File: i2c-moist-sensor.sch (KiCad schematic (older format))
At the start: 21 parts, among them IC1 ATTINY441-SSU, P1 CONN_02X03, X1 16MHz

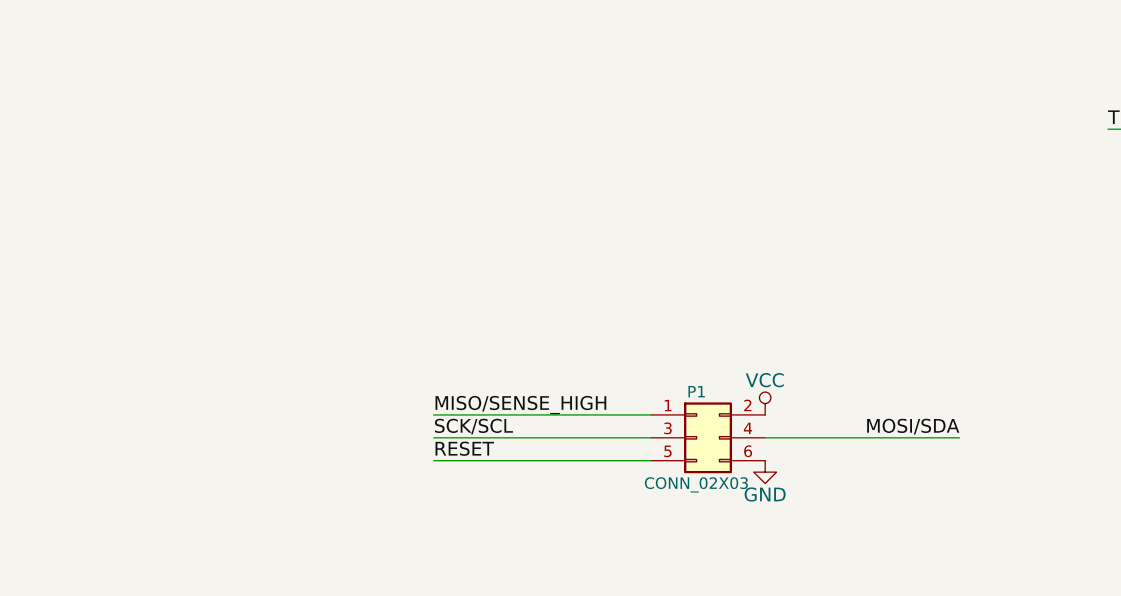
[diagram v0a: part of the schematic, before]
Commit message: Add Qwiic connectors
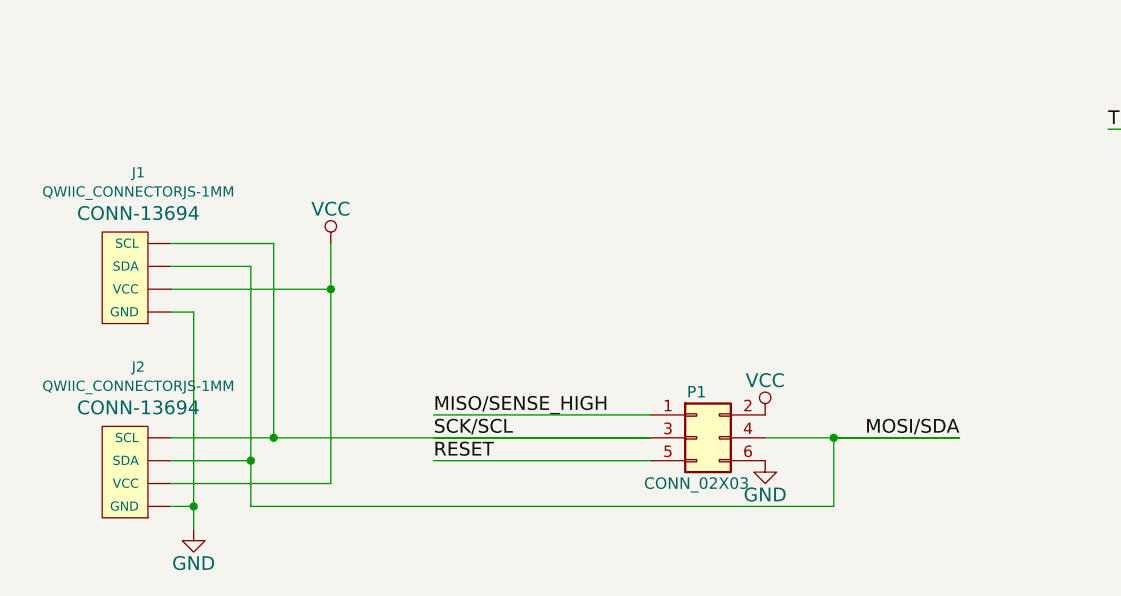
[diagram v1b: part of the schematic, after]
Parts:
- added J1, J2: QWIIC_CONNECTORJS-1MM, Connector_JST:JST_SH_SM04B-SRSS-TB_1x04-1MP_P1.00mm_Horizontal, symbol SparkFun-Connectors:QWIIC_CONNECTORJS-1MM
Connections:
- net GND: now also J1.1 (GND), J2.1 (GND)
- net MOSI/SDA: now also J1.3 (SDA), J2.3 (SDA)
- net SCK/SCL: now also J1.4 (SCL), J2.4 (SCL)
- net VCC: now also J1.2 (VCC), J2.2 (VCC)
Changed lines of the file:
@@
 	9600 3800 10500 3800
 Connection ~ 7250 4300
+$Comp
+L SparkFun-Connectors:QWIIC_CONNECTORJS-1MM J1
+U 1 1 5E00ADE6
+P 2050 5100
+F 0 "J1" H 2008 5710 45  0000 C CNN
+F 1 "QWIIC_CONNECTORJS-1MM" H 2008 5626 45  0000 C CNN
+F 2 "Connector_JST:JST_SH_SM04B-SRSS-TB_1x04-1MP_P1.00mm_Horizontal" H 2050 5600 20  0001 C CNN
+F 3 "" H 2050 5100 50  0001 C CNN
+F 4 "CONN-13694" H 2008 5531 60  0000 C CNN "Field4"
+	1    2050 5100
+	1    0    0    -1
+$EndComp
+$Comp
+L SparkFun-Connectors:QWIIC_CONNECTORJS-1MM J2
+U 1 1 5E00B3F3
+P 2050 5950
+F 0 "J2" H 2008 6560 45  0000 C CNN
+F 1 "QWIIC_CONNECTORJS-1MM" H 2008 6476 45  0000 C CNN
+F 2 "Connector_JST:JST_SH_SM04B-SRSS-TB_1x04-1MP_P1.00mm_Horizontal" H 2050 6450 20  0001 C CNN
+F 3 "" H 2050 5950 50  0001 C CNN
+F 4 "CONN-13694" H 2008 6381 60  0000 C CNN "Field4"
+	1    2050 5950
+	1    0    0    -1
+$EndComp
+$Comp
+L power:GND #PWR0101
+U 1 1 5E011E38
+P 2250 6050
+F 0 "#PWR0101" H 2250 5800 60  0001 C CNN
+F 1 "GND" H 2250 5900 60  0000 C CNN
+F 2 "" H 2250 6050 60  0000 C CNN
+F 3 "" H 2250 6050 60  0000 C CNN
+	1    2250 6050
+	1    0    0    -1
+$EndComp
+Wire Wire Line
+	2250 6050 2250 5950
+Wire Wire Line
+	2250 5950 2150 5950
+Wire Wire Line
+	2250 5950 2250 5100
+Wire Wire Line
+	2250 5100 2150 5100
+Connection ~ 2250 5950
+Wire Wire Line
+	2600 4800 2150 4800
+Wire Wire Line
+	2150 5650 2600 5650
+Wire Wire Line
+	5050 5650 5050 5950
+Wire Wire Line
+	5050 5950 2500 5950
+Wire Wire Line
+	2500 5950 2500 5750
+Wire Wire Line
+	2500 4900 2150 4900
+Connection ~ 5050 5650
+Wire Wire Line
+	5050 5650 5600 5650
+Wire Wire Line
+	2150 5750 2500 5750
+Connection ~ 2500 5750
+Wire Wire Line
+	2500 5750 2500 4900
+Wire Wire Line
+	2150 5850 2850 5850
+Wire Wire Line
+	2850 5850 2850 5000
+Wire Wire Line
+	2850 5000 2150 5000
+$Comp
+L power:VCC #PWR0102
+U 1 1 5E01C864
+P 2850 4800
+F 0 "#PWR0102" H 2850 4650 60  0001 C CNN
+F 1 "VCC" H 2850 4950 60  0000 C CNN
+F 2 "" H 2850 4800 60  0000 C CNN
+F 3 "" H 2850 4800 60  0000 C CNN
+	1    2850 4800
+	1    0    0    -1
+$EndComp
+Wire Wire Line
+	2850 4800 2850 5000
+Connection ~ 2850 5000
+Connection ~ 2600 5650
+Wire Wire Line
+	2600 4800 2600 5650
+Wire Wire Line
+	2600 5650 4250 5650
 Connection ~ 8500 3050
 Connection ~ 9300 2650
